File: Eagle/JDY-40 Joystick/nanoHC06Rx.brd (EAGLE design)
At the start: 99.3 x 52.1 mm, 22 parts

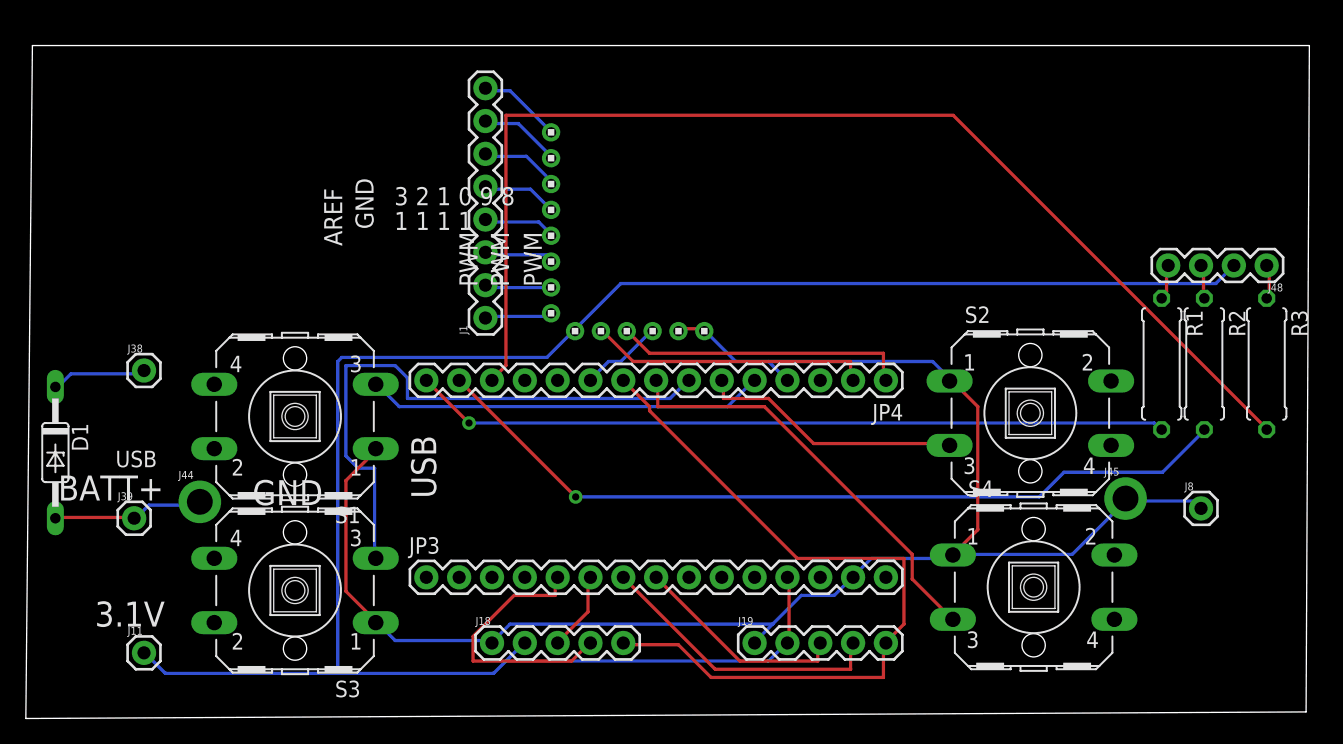
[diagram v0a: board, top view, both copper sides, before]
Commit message: Added Chrome App
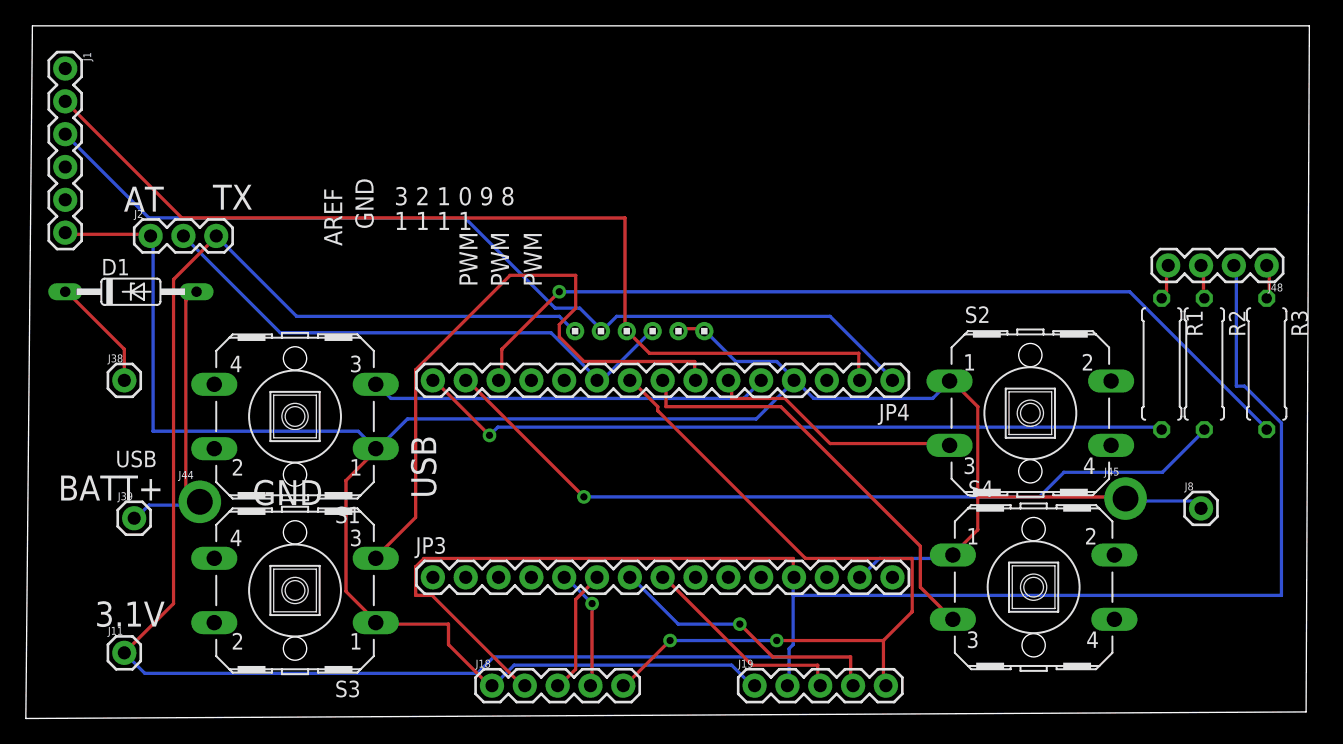
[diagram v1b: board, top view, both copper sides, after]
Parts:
- removed U$2: 1X8, headers(2mm):1X8
- added J2: (no value), SparkFun-Connectors:1X03
- J1: device SparkFun-Connectors:1X08 -> SparkFun-Connectors:1X06
- moved J1 37.8 mm to (3.05, 57.9), turned to 270 degrees
- moved D1 13.7 mm to (8.13, 40.6), turned to 0 degrees
- moved J18 3.30 mm to (36.1, 10.2)
- moved J19 3.30 mm to (56.4, 10.2)
- moved J38 1.70 mm to (7.62, 33.8)
- moved J11 1.52 mm to (7.62, 12.7)
- moved JP3 0.51 mm to (31.5, 18.5)
- moved JP4 0.51 mm to (67.1, 33.8)
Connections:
- removed net N$10: J1.6, U$2.6
- removed net N$11: J1.7, U$2.7
- removed net N$12: J1.8, U$2.8
- removed net N$5: J1.1, U$2.1
- removed net N$6: J1.2, U$2.2
- removed net N$7: J1.3, U$2.3
- removed net N$8: J1.4, U$2.4
- removed net N$9: J1.5, U$2.5
- net D7_D: now also J2.2
- net GND_D: now also J1.6, J2.1
- net RX_D: now also J1.3, JP4.1; no longer JP4.2
- net TX_D: now also J1.2, JP4.2; no longer JP4.1
- net VCC_D: now also J2.3
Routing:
- net VCC_D: track 155.2 -> 237.0 mm
- net GND_D: track 127.1 -> 188.1 mm
- net TX_D: track 22.7 -> 76.6 mm
- net RX_D: track 21.8 -> 73.0 mm
- net D7_D: track 6.39 -> 42.5 mm
- net D10_D: track 89.9 -> 68.0 mm, vias 0 -> 1
- net A1_D: track 20.7 -> 9.46 mm, vias 0 -> 1
- net BATT_3V3_D: track 11.8 -> 22.8 mm
- net N$12: track 6.63 -> 0.00 mm
- net N$11: track 6.47 -> 0.00 mm
- net N$10: track 6.30 -> 0.00 mm
- net N$9: track 5.94 -> 0.00 mm
- net N$8: track 5.78 -> 0.00 mm
- net N$7: track 5.61 -> 0.00 mm
- net N$5: track 5.45 -> 0.00 mm
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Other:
- board size 99.3 x 52.1 mm -> 99.3 x 53.6 mm
- board text added: "AT"
- board text added: "TX"

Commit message: websocket
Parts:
- moved J2 2.54 mm to (12.2, 45.0)
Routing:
- net VCC_D: track 237.0 -> 0.00 mm
- net GND_D: track 188.1 -> 0.00 mm
- net TX_D: track 76.6 -> 0.00 mm
- net RX_D: track 73.0 -> 0.00 mm
- net D10_D: track 68.0 -> 0.00 mm, vias 1 -> 0
- net D11_D: track 63.0 -> 0.00 mm, vias 1 -> 0
- net D6_D: track 60.2 -> 0.00 mm, vias 2 -> 0
- net D12_D: track 58.5 -> 0.00 mm, vias 1 -> 0
- net D4_D: track 49.3 -> 0.00 mm
- net D7_D: track 42.5 -> 0.00 mm
- net D5_D: track 33.1 -> 0.00 mm
- net D2_D: track 30.9 -> 0.00 mm
- net BATT_3V3_D: track 22.8 -> 0.00 mm
- net A3_D: track 22.0 -> 0.00 mm, vias 1 -> 0
- net D3_D: track 20.0 -> 0.00 mm
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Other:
- board text added: "RX"
